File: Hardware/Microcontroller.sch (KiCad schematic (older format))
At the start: 25 parts, among them J1 UPDI, J2 UART, J3 DCF77, J4 Vin, J5 HVReg, U3 ATtiny1606-S, U4 L78L05_SOT89, U5 DS3231MZ

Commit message: Reworked Schematic for GPS
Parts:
- removed C4: 100n, Capacitor_SMD:C_0603_1608Metric_Pad1.05x0.95mm_HandSolder, symbol Device:C_Small
- removed C5: 10n, Capacitor_SMD:C_0603_1608Metric_Pad1.05x0.95mm_HandSolder, symbol Device:C_Small
- removed R6, R9: 10k, Resistor_SMD:R_0603_1608Metric_Pad1.05x0.95mm_HandSolder, symbol Device:R_Small
- removed R7, R8: 4k7, Resistor_SMD:R_0603_1608Metric_Pad1.05x0.95mm_HandSolder, symbol Device:R_Small
- removed U5: DS3231MZ, Package_SO:SOIC-8_3.9x4.9mm_P1.27mm, symbol Timer_RTC:DS3231MZ
- added R? (x2): 100k, Resistor_SMD:R_0603_1608Metric_Pad1.05x0.95mm_HandSolder, symbol Device:R_Small
- J2: symbol Connector_Generic:Conn_01x03 -> Connector_Generic:Conn_01x02
- J3: value DCF77 -> NMEA; symbol Connector_Generic:Conn_01x03 -> Connector_Generic:Conn_01x06
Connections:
- net labels added: NMEA_RxD, NMEA_SYNC
- net labels removed: DCF77, RTC_SCL, RTC_SDA, RTC_SQW, UART_RxD
- wire segments 91 -> 67
- no-connect marks 9 -> 11
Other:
- note removed: "Real Time Clock"
- moved on the sheet: C8

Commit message: Start rework
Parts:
- J2: footprint Connector_PinHeader_2.54mm:PinHeader_1x03_P2.54mm_Vertical -> Connector_PinHeader_2.54mm:PinHeader_1x02_P2.54mm_Vertical
- J3: footprint DCF77:ELV_DCF-2_91610 -> Connector_PinHeader_1.00mm:PinHeader_1x06_P1.00mm_Vertical
- gave numbers to parts that had none: 2
- renumbered J5 to REG1
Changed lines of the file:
@@
 F 0 "J2" H 8480 4192 50  0000 L CNN
 F 1 "UART" H 8480 4101 50  0000 L CNN
-F 2 "Connector_PinHeader_2.54mm:PinHeader_1x03_P2.54mm_Vertical" H 8400 4150 50  0001 C CNN
+F 2 "Connector_PinHeader_2.54mm:PinHeader_1x02_P2.54mm_Vertical" H 8400 4150 50  0001 C CNN
 F 3 "~" H 8400 4150 50  0001 C CNN
 	1    8400 4150
@@
 F 0 "J3" H 8480 5092 50  0000 L CNN
 F 1 "NMEA" H 8480 5001 50  0000 L CNN
-F 2 "DCF77:ELV_DCF-2_91610" H 8400 5050 50  0001 C CNN
+F 2 "Connector_PinHeader_1.00mm:PinHeader_1x06_P1.00mm_Vertical" H 8400 5050 50  0001 C CNN
 F 3 "~" H 8400 5050 50  0001 C CNN
 	1    8400 5050
@@
 	5200 4350 5200 4450
 $Comp
-L Connector_Generic:Conn_01x03 J5
+L Connector_Generic:Conn_01x03 REG1
 U 1 1 5F7A5348
 P 10150 4500
-AR Path="/5F57C9A4/5F7A5348" Ref="J5"  Part="1"
+AR Path="/5F57C9A4/5F7A5348" Ref="REG1"  Part="1"
 AR Path="/5F63C067/5F7A5348" Ref="J?"  Part="1"
-F 0 "J5" H 10230 4542 50  0000 L CNN
+F 0 "REG1" H 10230 4542 50  0000 L CNN
 F 1 "HVReg" H 10230 4451 50  0000 L CNN
 F 2 "Nixies:NCH8200HV" H 10150 4500 50  0001 C CNN
@@
 NoConn ~ 8200 4850
 $Comp
-L Device:R_Small R?
+L Device:R_Small R7
 U 1 1 5FA68E9C
 P 7950 4950
-AR Path="/5F57C9A4/5FA68E9C" Ref="R?"  Part="1"
+AR Path="/5F57C9A4/5FA68E9C" Ref="R7"  Part="1"
 AR Path="/5F63C067/5FA68E9C" Ref="R?"  Part="1"
-F 0 "R?" V 7754 4950 50  0000 C CNN
+F 0 "R7" V 7754 4950 50  0000 C CNN
 F 1 "100k" V 7845 4950 50  0000 C CNN
 F 2 "Resistor_SMD:R_0603_1608Metric_Pad1.05x0.95mm_HandSolder" H 7950 4950 50  0001 C CNN
@@
 	7950 4800 8100 4800
 $Comp
-L Device:R_Small R?
+L Device:R_Small R6
 U 1 1 5FA77B0D
 P 7600 4950
-AR Path="/5F57C9A4/5FA77B0D" Ref="R?"  Part="1"
+AR Path="/5F57C9A4/5FA77B0D" Ref="R6"  Part="1"
 AR Path="/5F63C067/5FA77B0D" Ref="R?"  Part="1"
-F 0 "R?" V 7404 4950 50  0000 C CNN
+F 0 "R6" V 7404 4950 50  0000 C CNN
 F 1 "100k" V 7495 4950 50  0000 C CNN
 F 2 "Resistor_SMD:R_0603_1608Metric_Pad1.05x0.95mm_HandSolder" H 7600 4950 50  0001 C CNN

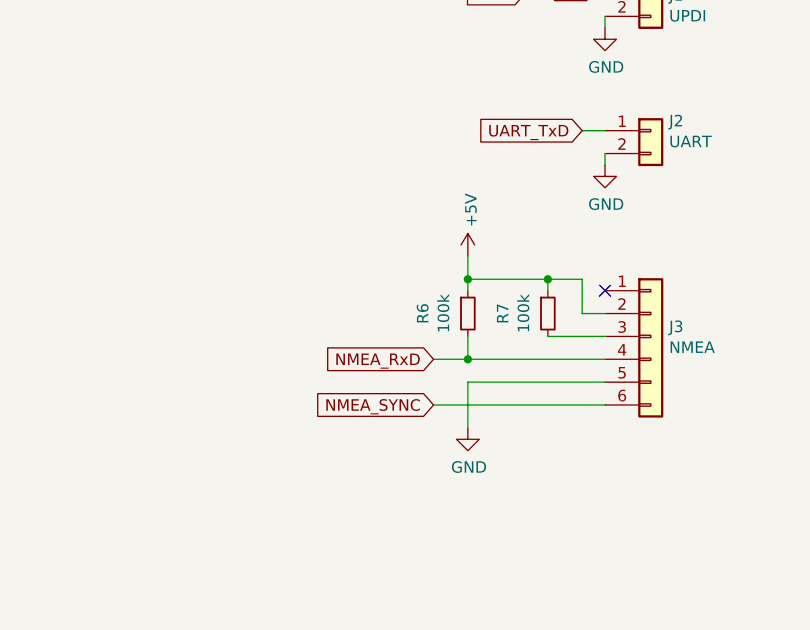
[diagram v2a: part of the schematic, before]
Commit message: Add signal inversion for NMEA
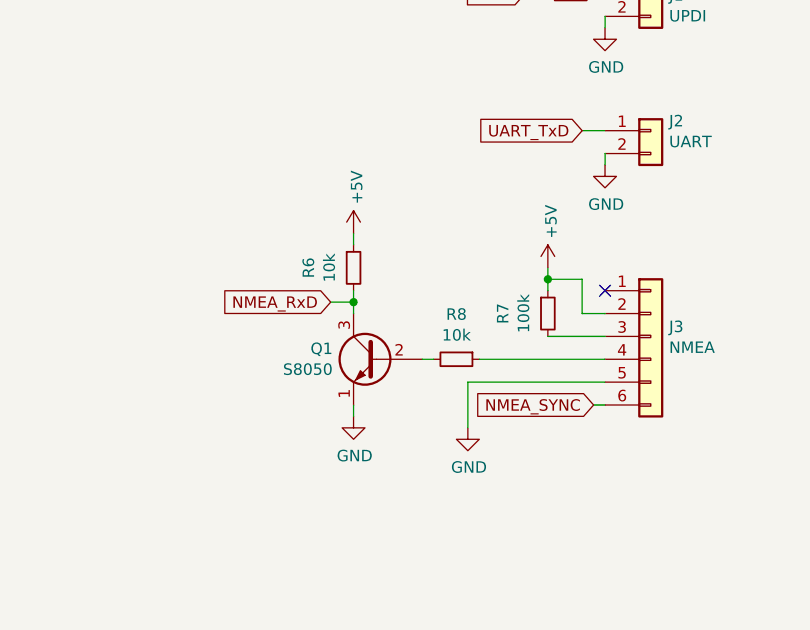
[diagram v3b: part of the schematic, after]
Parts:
- added Q1: S8050, Package_TO_SOT_THT:TO-92_Inline, symbol Transistor_BJT:S8050
- added R8: 10k, Resistor_SMD:R_0603_1608Metric_Pad1.05x0.95mm_HandSolder, symbol Device:R_Small
- R6: value 100k -> 10k
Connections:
- net GND: now also Q1.1 (E)
- net NMEA_RxD: now also Q1.3 (C); no longer J3.4 (Pin_4)
- new net: J3.4 (Pin_4), R8.1
- new net: Q1.2 (B), R8.2
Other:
- moved on the sheet: R6
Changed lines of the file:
@@
 L power:+5V #PWR?
 U 1 1 5F66ADEB
-P 7600 4700
+P 7950 4750
 AR Path="/5F8C807E/5F66ADEB" Ref="#PWR?"  Part="1"
 AR Path="/5F66ADEB" Ref="#PWR?"  Part="1"
@@
 AR Path="/5F63C067/5F66ADEB" Ref="#PWR?"  Part="1"
 AR Path="/5F645C82/5F66ADEB" Ref="#PWR?"  Part="1"
-F 0 "#PWR0118" H 7600 4550 50  0001 C CNN
-F 1 "+5V" V 7615 4828 50  0000 L CNN
-F 2 "" H 7600 4700 50  0001 C CNN
-F 3 "" H 7600 4700 50  0001 C CNN
-	1    7600 4700
+F 0 "#PWR0118" H 7950 4600 50  0001 C CNN
+F 1 "+5V" V 7965 4878 50  0000 L CNN
+F 2 "" H 7950 4750 50  0001 C CNN
+F 3 "" H 7950 4750 50  0001 C CNN
+	1    7950 4750
 	1    0    0    -1
 $EndComp
@@
 Text GLabel 1450 2600 0    50   Input ~ 0
 NMEA_SYNC
-Text GLabel 7450 5350 0    50   Input ~ 0
+Text GLabel 8150 5350 0    50   Input ~ 0
 NMEA_SYNC
-Text GLabel 7450 5150 0    50   Input ~ 0
+Text GLabel 7000 4900 0    50   Input ~ 0
 NMEA_RxD
 Wire Wire Line
-	8200 5350 7450 5350
+	8200 5350 8150 5350
 NoConn ~ 8200 4850
 $Comp
@@
 	7600 5250 8200 5250
 Wire Wire Line
-	7600 4700 7600 4800
-Wire Wire Line
-	7600 4800 7950 4800
-Wire Wire Line
 	8100 4800 8100 4950
 Wire Wire Line
 	7950 4850 7950 4800
-Connection ~ 7950 4800
 Wire Wire Line
 	7950 4800 8100 4800
@@
 L Device:R_Small R6
 U 1 1 5FA77B0D
-P 7600 4950
+P 7100 4750
 AR Path="/5F57C9A4/5FA77B0D" Ref="R6"  Part="1"
 AR Path="/5F63C067/5FA77B0D" Ref="R?"  Part="1"
-F 0 "R6" V 7404 4950 50  0000 C CNN
-F 1 "100k" V 7495 4950 50  0000 C CNN
-F 2 "Resistor_SMD:R_0603_1608Metric_Pad1.05x0.95mm_HandSolder" H 7600 4950 50  0001 C CNN
-F 3 "~" H 7600 4950 50  0001 C CNN
-	1    7600 4950
-	1    0    0    -1
-$EndComp
-Wire Wire Line
-	7450 5150 7600 5150
-Wire Wire Line
-	7600 4800 7600 4850
-Connection ~ 7600 4800
-Wire Wire Line
-	7600 5050 7600 5150
-Connection ~ 7600 5150
-Wire Wire Line
-	7600 5150 8200 5150
+F 0 "R6" V 6904 4750 50  0000 C CNN
+F 1 "10k" V 6995 4750 50  0000 C CNN
+F 2 "Resistor_SMD:R_0603_1608Metric_Pad1.05x0.95mm_HandSolder" H 7100 4750 50  0001 C CNN
+F 3 "~" H 7100 4750 50  0001 C CNN
+	1    7100 4750
+	1    0    0    -1
+$EndComp
 Wire Wire Line
 	7950 5050 8200 5050
@@
 NoConn ~ 2750 2400
 NoConn ~ 2750 1700
+$Comp
+L Transistor_BJT:S8050 Q1
+U 1 1 5FA6306F
+P 7200 5150
+F 0 "Q1" H 7391 5196 50  0000 L CNN
+F 1 "S8050" H 7391 5105 50  0000 L CNN
+F 2 "Package_TO_SOT_THT:TO-92_Inline" H 7400 5075 50  0001 L CIN
+F 3 "http://www.unisonic.com.tw/datasheet/S8050.pdf" H 7200 5150 50  0001 L CNN
+	1    7200 5150
+	-1   0    0    -1
+$EndComp
+$Comp
+L Device:R_Small R8
+U 1 1 5FA67166
+P 7550 5150
+AR Path="/5F57C9A4/5FA67166" Ref="R8"  Part="1"
+AR Path="/5F63C067/5FA67166" Ref="R?"  Part="1"
+F 0 "R8" V 7354 5150 50  0000 C CNN
+F 1 "10k" V 7445 5150 50  0000 C CNN
+F 2 "Resistor_SMD:R_0603_1608Metric_Pad1.05x0.95mm_HandSolder" H 7550 5150 50  0001 C CNN
+F 3 "~" H 7550 5150 50  0001 C CNN
+	1    7550 5150
+	0    1    1    0
+$EndComp
+Wire Wire Line
+	7100 4900 7000 4900
+$Comp
+L power:GND #PWR?
+U 1 1 5FA6D91E
+P 7100 5400
+AR Path="/5F8C807E/5FA6D91E" Ref="#PWR?"  Part="1"
+AR Path="/5FA6D91E" Ref="#PWR?"  Part="1"
+AR Path="/5F57C9A4/5FA6D91E" Ref="#PWR0115"  Part="1"
+AR Path="/5F57DBA0/5FA6D91E" Ref="#PWR?"  Part="1"
+AR Path="/5F63C067/5FA6D91E" Ref="#PWR?"  Part="1"
+AR Path="/5F645C82/5FA6D91E" Ref="#PWR?"  Part="1"
+F 0 "#PWR0115" H 7100 5150 50  0001 C CNN
+F 1 "GND" H 7105 5227 50  0000 C CNN
+F 2 "" H 7100 5400 50  0001 C CNN
+F 3 "" H 7100 5400 50  0001 C CNN
+	1    7100 5400
+	1    0    0    -1
+$EndComp
+Wire Wire Line
+	7650 5150 8200 5150
+Wire Wire Line
+	7450 5150 7400 5150
+Wire Wire Line
+	7100 4850 7100 4900
+$Comp
+L power:+5V #PWR?
+U 1 1 5FA89842
+P 7100 4600
+AR Path="/5F8C807E/5FA89842" Ref="#PWR?"  Part="1"
+AR Path="/5FA89842" Ref="#PWR?"  Part="1"
+AR Path="/5F57C9A4/5FA89842" Ref="#PWR?"  Part="1"
+AR Path="/5F57DBA0/5FA89842" Ref="#PWR?"  Part="1"
+AR Path="/5F63C067/5FA89842" Ref="#PWR?"  Part="1"
+AR Path="/5F645C82/5FA89842" Ref="#PWR?"  Part="1"
+F 0 "#PWR?" H 7100 4450 50  0001 C CNN
+F 1 "+5V" V 7115 4728 50  0000 L CNN
+F 2 "" H 7100 4600 50  0001 C CNN
+F 3 "" H 7100 4600 50  0001 C CNN
+	1    7100 4600
+	1    0    0    -1
+$EndComp
+Wire Wire Line
+	7100 4600 7100 4650
+Wire Wire Line
+	7950 4750 7950 4800
+Connection ~ 7950 4800
+Wire Wire Line
+	7100 5350 7100 5400
+Connection ~ 7100 4900
+Wire Wire Line
+	7100 4900 7100 4950
 $EndSCHEMATC

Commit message: Fix packages, route left nixies
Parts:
- C3, C6, C7: footprint Capacitor_SMD:C_0603_1608Metric_Pad1.05x0.95mm_HandSolder -> Capacitor_SMD:C_0603_1608Metric
- C8: footprint Capacitor_SMD:C_0805_2012Metric_Pad1.15x1.40mm_HandSolder -> Capacitor_SMD:C_0805_2012Metric
- F2: footprint Fuse:Fuse_0603_1608Metric_Pad1.05x0.95mm_HandSolder -> Fuse:Fuse_0603_1608Metric
- Q1: footprint Package_TO_SOT_THT:TO-92_Inline -> Package_TO_SOT_SMD:SOT-23
- R5, R6, R7, R8: footprint Resistor_SMD:R_0603_1608Metric_Pad1.05x0.95mm_HandSolder -> Resistor_SMD:R_0603_1608Metric
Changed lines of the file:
@@
 F 0 "C3" H 842 7246 50  0000 L CNN
 F 1 "100n" H 842 7155 50  0000 L CNN
-F 2 "Capacitor_SMD:C_0603_1608Metric_Pad1.05x0.95mm_HandSolder" H 750 7200 50  0001 C CNN
+F 2 "Capacitor_SMD:C_0603_1608Metric" H 750 7200 50  0001 C CNN
 F 3 "~" H 750 7200 50  0001 C CNN
 	1    750  7200
@@
 F 0 "R5" V 7854 3550 50  0000 C CNN
 F 1 "470" V 7945 3550 50  0000 C CNN
-F 2 "Resistor_SMD:R_0603_1608Metric_Pad1.05x0.95mm_HandSolder" H 8050 3550 50  0001 C CNN
+F 2 "Resistor_SMD:R_0603_1608Metric" H 8050 3550 50  0001 C CNN
 F 3 "~" H 8050 3550 50  0001 C CNN
 	1    8050 3550
@@
 F 0 "C6" H 4192 4796 50  0000 L CNN
 F 1 "330n" H 4192 4705 50  0000 L CNN
-F 2 "Capacitor_SMD:C_0603_1608Metric_Pad1.05x0.95mm_HandSolder" H 4100 4750 50  0001 C CNN
+F 2 "Capacitor_SMD:C_0603_1608Metric" H 4100 4750 50  0001 C CNN
 F 3 "~" H 4100 4750 50  0001 C CNN
 	1    4100 4750
@@
 F 0 "C7" H 5292 4796 50  0000 L CNN
 F 1 "100n" H 5292 4705 50  0000 L CNN
-F 2 "Capacitor_SMD:C_0603_1608Metric_Pad1.05x0.95mm_HandSolder" H 5200 4750 50  0001 C CNN
+F 2 "Capacitor_SMD:C_0603_1608Metric" H 5200 4750 50  0001 C CNN
 F 3 "~" H 5200 4750 50  0001 C CNN
 	1    5200 4750
@@
 F 0 "C8" H 1242 7246 50  0000 L CNN
 F 1 "10u" H 1242 7155 50  0000 L CNN
-F 2 "Capacitor_SMD:C_0805_2012Metric_Pad1.15x1.40mm_HandSolder" H 1150 7200 50  0001 C CNN
+F 2 "Capacitor_SMD:C_0805_2012Metric" H 1150 7200 50  0001 C CNN
 F 3 "~" H 1150 7200 50  0001 C CNN
 	1    1150 7200
@@
 F 0 "F2" H 3750 4635 50  0000 C CNN
 F 1 "200mA" H 3750 4544 50  0000 C CNN
-F 2 "Fuse:Fuse_0603_1608Metric_Pad1.05x0.95mm_HandSolder" H 3750 4450 50  0001 C CNN
+F 2 "Fuse:Fuse_0603_1608Metric" H 3750 4450 50  0001 C CNN
 F 3 "~" H 3750 4450 50  0001 C CNN
 	1    3750 4450
@@
 F 0 "R7" V 7754 4950 50  0000 C CNN
 F 1 "100k" V 7845 4950 50  0000 C CNN
-F 2 "Resistor_SMD:R_0603_1608Metric_Pad1.05x0.95mm_HandSolder" H 7950 4950 50  0001 C CNN
+F 2 "Resistor_SMD:R_0603_1608Metric" H 7950 4950 50  0001 C CNN
 F 3 "~" H 7950 4950 50  0001 C CNN
 	1    7950 4950
@@
 F 0 "R6" V 6904 4750 50  0000 C CNN
 F 1 "10k" V 6995 4750 50  0000 C CNN
-F 2 "Resistor_SMD:R_0603_1608Metric_Pad1.05x0.95mm_HandSolder" H 7100 4750 50  0001 C CNN
+F 2 "Resistor_SMD:R_0603_1608Metric" H 7100 4750 50  0001 C CNN
 F 3 "~" H 7100 4750 50  0001 C CNN
 	1    7100 4750
@@
 F 0 "Q1" H 7391 5196 50  0000 L CNN
 F 1 "S8050" H 7391 5105 50  0000 L CNN
-F 2 "Package_TO_SOT_THT:TO-92_Inline" H 7400 5075 50  0001 L CIN
+F 2 "Package_TO_SOT_SMD:SOT-23" H 7400 5075 50  0001 L CIN
 F 3 "http://www.unisonic.com.tw/datasheet/S8050.pdf" H 7200 5150 50  0001 L CNN
 	1    7200 5150
@@
 F 0 "R8" V 7354 5150 50  0000 C CNN
 F 1 "10k" V 7445 5150 50  0000 C CNN
-F 2 "Resistor_SMD:R_0603_1608Metric_Pad1.05x0.95mm_HandSolder" H 7550 5150 50  0001 C CNN
+F 2 "Resistor_SMD:R_0603_1608Metric" H 7550 5150 50  0001 C CNN
 F 3 "~" H 7550 5150 50  0001 C CNN
 	1    7550 5150
@@
 AR Path="/5F8C807E/5FA89842" Ref="#PWR?"  Part="1"
 AR Path="/5FA89842" Ref="#PWR?"  Part="1"
-AR Path="/5F57C9A4/5FA89842" Ref="#PWR?"  Part="1"
+AR Path="/5F57C9A4/5FA89842" Ref="#PWR0116"  Part="1"
 AR Path="/5F57DBA0/5FA89842" Ref="#PWR?"  Part="1"
 AR Path="/5F63C067/5FA89842" Ref="#PWR?"  Part="1"
 AR Path="/5F645C82/5FA89842" Ref="#PWR?"  Part="1"
-F 0 "#PWR?" H 7100 4450 50  0001 C CNN
+F 0 "#PWR0116" H 7100 4450 50  0001 C CNN
 F 1 "+5V" V 7115 4728 50  0000 L CNN
 F 2 "" H 7100 4600 50  0001 C CNN

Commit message: More layouting
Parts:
- J3: footprint Connector_PinHeader_1.00mm:PinHeader_1x06_P1.00mm_Vertical -> Connector_PinHeader_1.27mm:PinHeader_1x06_P1.27mm_Vertical
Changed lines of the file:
@@
 F 0 "J3" H 8480 5092 50  0000 L CNN
 F 1 "NMEA" H 8480 5001 50  0000 L CNN
-F 2 "Connector_PinHeader_1.00mm:PinHeader_1x06_P1.00mm_Vertical" H 8400 5050 50  0001 C CNN
+F 2 "Connector_PinHeader_1.27mm:PinHeader_1x06_P1.27mm_Vertical" H 8400 5050 50  0001 C CNN
 F 3 "~" H 8400 5050 50  0001 C CNN
 	1    8400 5050

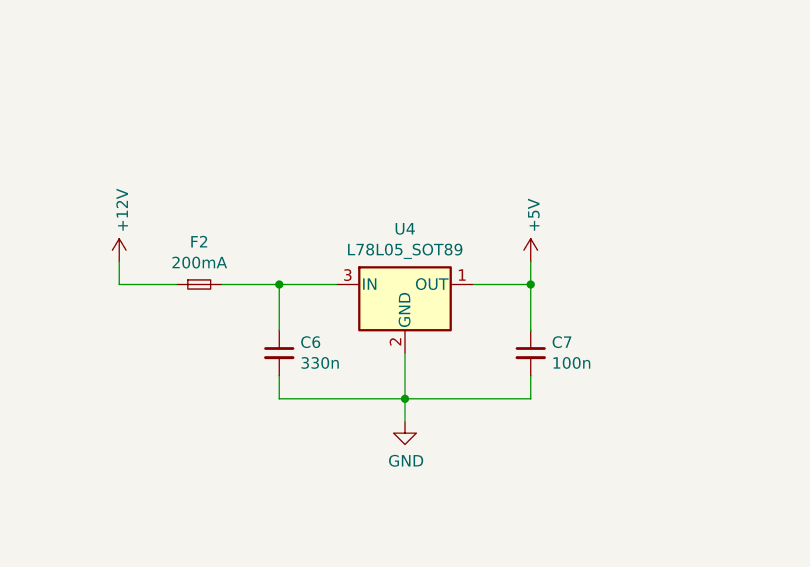
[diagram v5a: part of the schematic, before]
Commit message: Replace LDO
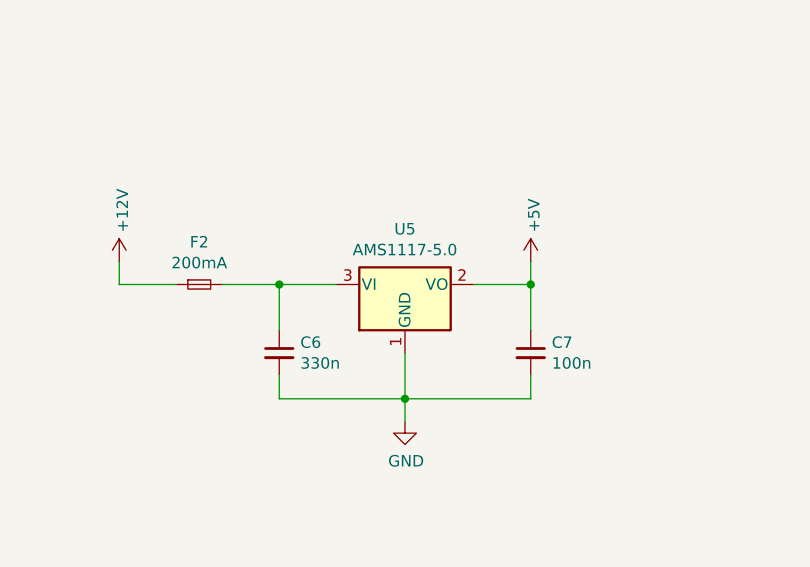
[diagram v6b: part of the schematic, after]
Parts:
- removed U4: L78L05_SOT89, Package_TO_SOT_SMD:SOT-89-3, symbol Regulator_Linear:L78L05_SOT89
- added U5: AMS1117-5.0, Package_TO_SOT_SMD:SOT-223-3_TabPin2, symbol Regulator_Linear:AMS1117-5.0
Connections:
- net +5V: now also U5.2 (VO)
- net GND: now also U5.1 (GND)
- net at C6.1, F2.2: now also U5.3 (VI)
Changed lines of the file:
@@
-$EndComp
-$Comp
-L Regulator_Linear:L78L05_SOT89 U4
-U 1 1 5F682BAE
-P 4650 4450
-F 0 "U4" H 4650 4692 50  0000 C CNN
-F 1 "L78L05_SOT89" H 4650 4601 50  0000 C CNN
-F 2 "Package_TO_SOT_SMD:SOT-89-3" H 4650 4650 50  0001 C CIN
-F 3 "http://www.st.com/content/ccc/resource/technical/document/datasheet/15/55/e5/aa/23/5b/43/fd/CD00000446.pdf/files/CD00000446.pdf/jcr:content/translations/en.CD00000446.pdf" H 4650 4400 50  0001 C CNN
-	1    4650 4450
-	1    0    0    -1
 $EndComp
 $Comp
@@
 	4100 4650 4100 4450
 Wire Wire Line
-	4100 4450 4350 4450
-Wire Wire Line
 	3400 4350 3400 4450
 Connection ~ 5200 4450
@@
 Wire Wire Line
 	3850 4450 4100 4450
-Connection ~ 4100 4450
 Text GLabel 1450 2600 0    50   Input ~ 0
 NMEA_SYNC
@@
 Wire Wire Line
 	7100 4900 7100 4950
+$Comp
+L Regulator_Linear:AMS1117-5.0 U5
+U 1 1 5FA81909
+P 4650 4450
+F 0 "U5" H 4650 4692 50  0000 C CNN
+F 1 "AMS1117-5.0" H 4650 4601 50  0000 C CNN
+F 2 "Package_TO_SOT_SMD:SOT-223-3_TabPin2" H 4650 4650 50  0001 C CNN
+F 3 "http://www.advanced-monolithic.com/pdf/ds1117.pdf" H 4750 4200 50  0001 C CNN
+	1    4650 4450
+	1    0    0    -1
+$EndComp
+Connection ~ 4100 4450
+Wire Wire Line
+	4100 4450 4350 4450
 $EndSCHEMATC
